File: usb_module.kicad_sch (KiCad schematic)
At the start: 10 parts, among them J1 USB_C_Receptacle_USB2.0_14P, U3 USBLC6-2P6

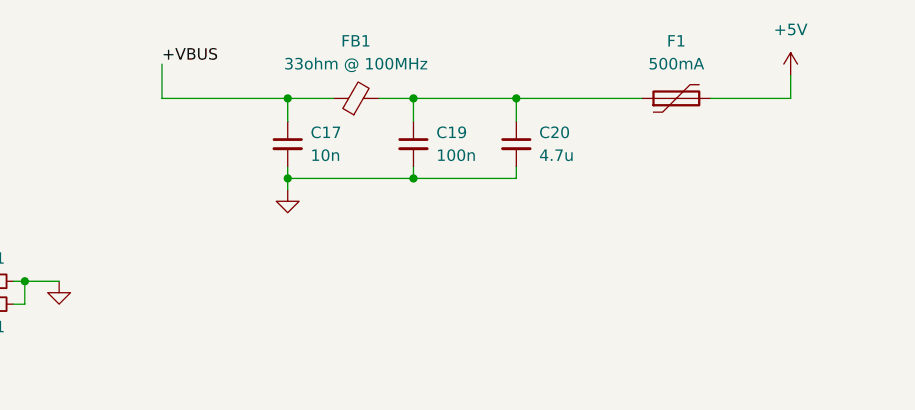
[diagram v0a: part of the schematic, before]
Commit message: Redesigned power supply. First board draft
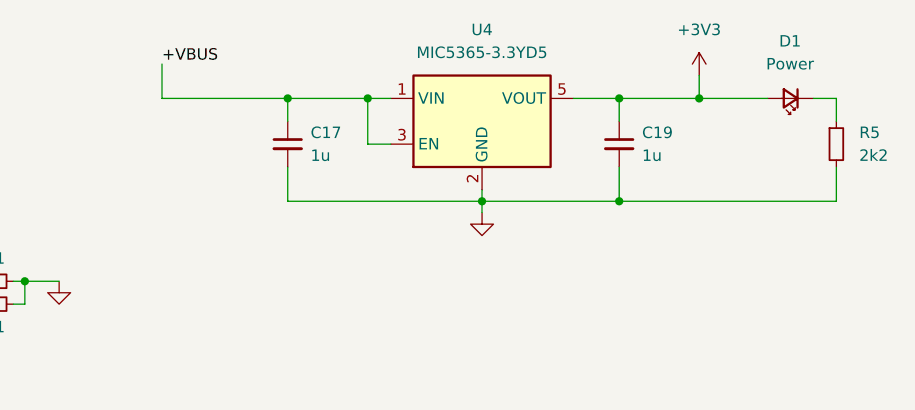
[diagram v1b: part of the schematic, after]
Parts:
- removed C20: 4.7u, Capacitor_SMD:C_0402_1005Metric, symbol Device:C_Small
- removed F1: 500mA, Capacitor_SMD:C_1206_3216Metric, symbol Device:Polyfuse
- removed FB1: 33ohm @ 100MHz, Inductor_SMD:L_0402_1005Metric, symbol Device:FerriteBead_Small
- added D1: Power, LED_SMD:LED_0603_1608Metric, symbol Device:LED_Small
- added R5: 2k2, Resistor_SMD:R_0402_1005Metric, symbol Device:R_Small
- added U4: MIC5365-3.3YD5, Package_TO_SOT_SMD:SOT-23-5, symbol Regulator_Linear:MIC5365-3.3YD5
- C17: value 10n -> 1u
- C19: value 100n -> 1u
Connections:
- net +VBUS: now also U4.1 (VIN), U4.3 (EN)
- net GND: now also R5.2, U4.2 (GND)
- net +3V3: now reaches C19.1
- net +3V3: now also D1.2 (A), U4.5 (VOUT)
- new net: D1.1 (K), R5.1

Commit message: BOM assigned
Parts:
- removed U4: MIC5365-3.3YD5, Package_TO_SOT_SMD:SOT-23-5, symbol Regulator_Linear:MIC5365-3.3YD5
- added U5: MIC5365-3.3YC5, Package_TO_SOT_SMD:SOT-353_SC-70-5, symbol Regulator_Linear:MIC5365-3.3YC5
- C17, C19: LCSC (none) -> C52923
- C18: LCSC (none) -> C1525
- D1: LCSC (none) -> C2286
- J1: LCSC (none) -> C319148
- R2, R3: LCSC (none) -> C25905
- R5: LCSC (none) -> C25879
- U3: LCSC (none) -> C2827693
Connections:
- net +3V3: now also U5.5 (VOUT)
- net +VBUS: now also U5.1 (VIN), U5.3 (EN)
- net GND: now also U5.2 (GND)
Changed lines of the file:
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@@
+			)
+		)
+		(property "LCSC" "C2827693"
+			(at 105.41 88.9 0)
+			(effects
+				(font
+					(size 1.27 1.27)
+				)
+				(hide yes)
 			)
 		)
@@
 			)
 		)
+		(property "LCSC" "C2286"
+			(at 189.23 33.02 0)
+			(effects
+				(font
+					(size 1.27 1.27)
+				)
+				(hide yes)
+			)
+		)
 		(pin "2"
 		)
@@
 				(path "/75856061-4be0-4eb9-8c9e-0f2487affa58/300908a8-4daf-42bb-995e-ad716e8a0f18"
 					(reference "D1")
-					(unit 1)
-				)
-			)
-		)
-	)
-	(symbol
-		(lib_id "Regulator_Linear:MIC5365-3.3YD5")
-		(at 154.94 35.56 0)
-		(unit 1)
-		(exclude_from_sim no)
-		(in_bom yes)
-		(on_board yes)
-		(dnp no)
-		(fields_autoplaced yes)
-		(property "Reference" "U4"
-			(at 154.94 25.4 0)
-			(effects
-				(font
-					(size 1.27 1.27)
-				)
-			)
-		)
-		(property "Value" "MIC5365-3.3YD5"
-			(at 154.94 27.94 0)
-			(effects
-				(font
-					(size 1.27 1.27)
-				)
-			)
-		)
-		(property "Footprint" "Package_TO_SOT_SMD:SOT-23-5"
-			(at 154.94 26.67 0)
-			(effects
-				(font
-					(size 1.27 1.27)
-				)
-				(hide yes)
-			)
-		)
-		(property "Datasheet" "http://ww1.microchip.com/downloads/en/DeviceDoc/mic5365.pdf"
-			(at 148.59 29.21 0)
-			(effects
-				(font
-					(size 1.27 1.27)
-				)
-				(hide yes)
-			)
-		)
-		(property "Description" "150mA Low-dropout Voltage Regulator, Vout 3.3V, Vin up to 5.5V, SOT-23-5"
-			(at 154.94 35.56 0)
-			(effects
-				(font
-					(size 1.27 1.27)
-				)
-				(hide yes)
-			)
-		)
-		(pin "3"
-		)
-		(pin "1"
-		)
-		(pin "2"
-		)
-		(pin "4"
-		)
-		(pin "5"
-		)
-		(instances
-			(project ""
-				(path "/75856061-4be0-4eb9-8c9e-0f2487affa58/300908a8-4daf-42bb-995e-ad716e8a0f18"
-					(reference "U4")
 					(unit 1)
 				)
@@
 			)
 		)
+		(property "LCSC" "C25905"
+			(at 100.33 55.88 90)
+			(effects
+				(font
+					(size 1.27 1.27)
+				)
+				(hide yes)
+			)
+		)
 		(pin "2"
 		)
@@
 			)
 		)
+		(property "LCSC" "C319148"
+			(at 53.34 63.5 0)
+			(effects
+				(font
+					(size 1.27 1.27)
+				)
+				(hide yes)
+			)
+		)
 		(pin "B6"
 		)
@@
 				(path "/75856061-4be0-4eb9-8c9e-0f2487affa58/300908a8-4daf-42bb-995e-ad716e8a0f18"
 					(reference "J1")
+					(unit 1)
+				)
+			)
+		)
+	)
+	(symbol
+		(lib_id "Regulator_Linear:MIC5365-3.3YC5")
+		(at 154.94 35.56 0)
+		(unit 1)
+		(exclude_from_sim no)
+		(in_bom yes)
+		(on_board yes)
+		(dnp no)
+		(fields_autoplaced yes)
+		(property "Reference" "U5"
+			(at 154.94 25.4 0)
+			(effects
+				(font
+					(size 1.27 1.27)
+				)
+			)
+		)
+		(property "Value" "MIC5365-3.3YC5"
+			(at 154.94 27.94 0)
+			(effects
+				(font
+					(size 1.27 1.27)
+				)
+			)
+		)
+		(property "Footprint" "Package_TO_SOT_SMD:SOT-353_SC-70-5"
+			(at 154.94 26.67 0)
+			(effects
+				(font
+					(size 1.27 1.27)
+				)
+				(hide yes)
+			)
+		)
+		(property "Datasheet" "http://ww1.microchip.com/downloads/en/DeviceDoc/mic5365.pdf"
+			(at 147.32 15.24 0)
+			(effects
+				(font
+					(size 1.27 1.27)
+				)
+				(hide yes)
+			)
+		)
+		(property "Description" "150mA Low-dropout Voltage Regulator, Vout 3.3V, Vin up to 5.5V, SC-70-5"
+			(at 154.94 35.56 0)
+			(effects
+				(font
+					(size 1.27 1.27)
+				)
+				(hide yes)
+			)
+		)
+		(property "LCSC" "C3021118"
+			(at 154.94 35.56 0)
+			(effects
+				(font
+					(size 1.27 1.27)
+				)
+				(hide yes)
+			)
+		)
+		(pin "1"
+		)
+		(pin "3"
+		)
+		(pin "4"
+		)
+		(pin "2"
+		)
+		(pin "5"
+		)
+		(instances
+			(project ""
+				(path "/75856061-4be0-4eb9-8c9e-0f2487affa58/300908a8-4daf-42bb-995e-ad716e8a0f18"
+					(reference "U5")
 					(unit 1)
 				)
@@
 			)
 		)
+		(property "LCSC" "C25879"
+			(at 194.31 38.1 0)
+			(effects
+				(font
+					(size 1.27 1.27)
+				)
+				(hide yes)
+			)
+		)
 		(pin "1"
 		)
@@
 			)
 		)
+		(property "LCSC" "C25905"
+			(at 100.33 53.34 90)
+			(effects
+				(font
+					(size 1.27 1.27)
+				)
+				(hide yes)
+			)
+		)
 		(pin "2"
 		)
@@
 			)
 		)
+		(property "LCSC" "C52923"
+			(at 170.18 38.1 0)
+			(effects
+				(font
+					(size 1.27 1.27)
+				)
+				(hide yes)
+			)
+		)
 		(pin "1"
 		)
@@
 		)
 		(property "Description" "Unpolarized capacitor, small symbol"
+			(at 83.82 90.17 0)
+			(effects
+				(font
+					(size 1.27 1.27)
+				)
+				(hide yes)
+			)
+		)
+		(property "LCSC" "C1525"
 			(at 83.82 90.17 0)
 			(effects
@@
 			(at 133.35 38.1 0)
 			(effects
+				(font
+					(size 1.27 1.27)
+				)
+				(hide yes)
+			)
+		)
+		(property "LCSC" "C52923"
+			(at 133.35 38.1 0)
+			(effects

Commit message: Minor changes
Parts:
- C17, C19: LCSC C52923 -> (none); MPN (none) -> C52923
- C18: LCSC C1525 -> (none); MPN (none) -> C1525
- D1: LCSC C2286 -> (none); MPN (none) -> C2286
- J1: JLCPCB Position Offset (none) -> 0,1.4605; LCSC C319148 -> (none); MPN (none) -> C319148
- R2, R3: LCSC C25905 -> (none); MPN (none) -> C25905
- R5: LCSC C25879 -> (none); MPN (none) -> C25879
- U3: JLCPCB Rotation Offset (none) -> -90; LCSC C2827693 -> (none); MPN (none) -> C2827693
- U5: LCSC C3021118 -> (none); MPN (none) -> C3021118
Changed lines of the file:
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@@
 			)
 		)
-		(property "LCSC" "C2827693"
+		(property "MPN" "C2827693"
+			(at 105.41 88.9 0)
+			(effects
+				(font
+					(size 1.27 1.27)
+				)
+				(hide yes)
+			)
+		)
+		(property "JLCPCB Rotation Offset" "-90"
 			(at 105.41 88.9 0)
 			(effects
@@
 			)
 		)
-		(property "LCSC" "C2286"
+		(property "MPN" "C2286"
 			(at 189.23 33.02 0)
 			(effects
@@
 			)
 		)
-		(property "LCSC" "C25905"
+		(property "MPN" "C25905"
 			(at 100.33 55.88 90)
 			(effects
@@
 			)
 		)
-		(property "LCSC" "C319148"
+		(property "MPN" "C319148"
+			(at 53.34 63.5 0)
+			(effects
+				(font
+					(size 1.27 1.27)
+				)
+				(hide yes)
+			)
+		)
+		(property "JLCPCB Position Offset" "0,1.4605"
 			(at 53.34 63.5 0)
 			(effects
@@
 			)
 		)
-		(property "LCSC" "C3021118"
+		(property "MPN" "C3021118"
 			(at 154.94 35.56 0)
 			(effects
@@
 			)
 		)
-		(property "LCSC" "C25879"
+		(property "MPN" "C25879"
 			(at 194.31 38.1 0)
 			(effects
@@
 			)
 		)
-		(property "LCSC" "C25905"
+		(property "MPN" "C25905"
 			(at 100.33 53.34 90)
 			(effects
@@
 			)
 		)
-		(property "LCSC" "C52923"
+		(property "MPN" "C52923"
 			(at 170.18 38.1 0)
 			(effects
@@
 			)
 		)
-		(property "LCSC" "C1525"
+		(property "MPN" "C1525"
 			(at 83.82 90.17 0)
 			(effects
@@
 			)
 		)
-		(property "LCSC" "C52923"
+		(property "MPN" "C52923"
 			(at 133.35 38.1 0)
 			(effects
